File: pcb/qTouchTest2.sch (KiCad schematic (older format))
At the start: 40 parts, among them CON1 AVR-ISP-6, J1 USB-MINI-B, K1 CONN_3, P1 CONN_1, P2 CONN_1, P3 CONN_1, P6 CONN_1, P7 CONN_1, P8 CONN_1, P9 CONN_1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

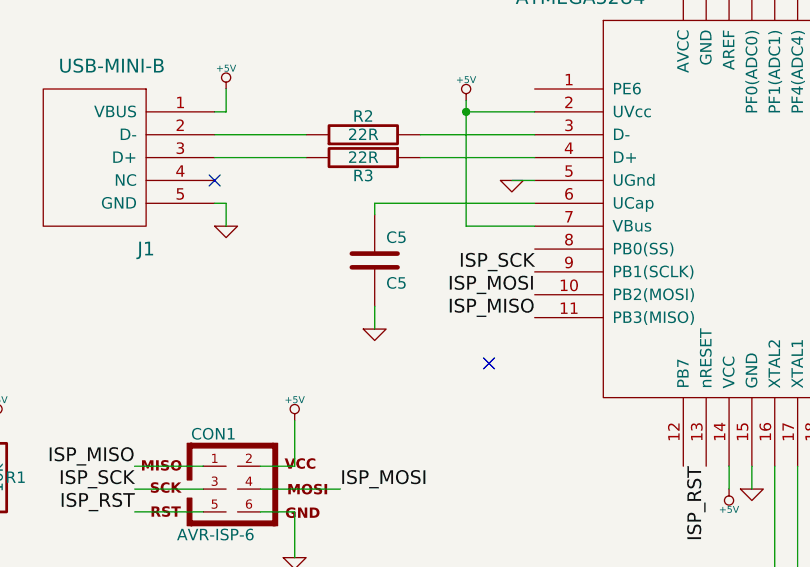
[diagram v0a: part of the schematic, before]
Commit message: adding C5 value to schematic and netlist
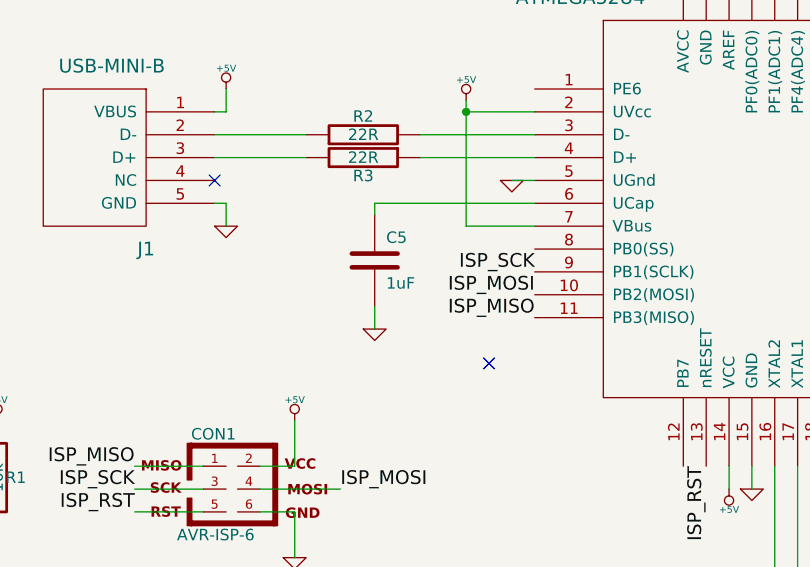
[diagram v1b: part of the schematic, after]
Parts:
- C5: value C5 -> 1uF
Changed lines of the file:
@@
-EESchema Schematic File Version 2  date Fri 04 May 2012 02:13:05 PM EEST
+EESchema Schematic File Version 2  date Wed 27 Mar 2013 18:11:13 GMT
 LIBS:power
 LIBS:device
@@
 LIBS:contrib
 LIBS:valves
-LIBS:my_parts
 LIBS:qTouchTest2-cache
 EELAYER 25  0
@@
 Sheet 1 1
 Title ""
-Date "4 may 2012"
+Date "27 mar 2013"
 Rev ""
 Comp ""
@@
 P 4050 3600
 F 0 "C5" H 4100 3700 50  0000 L CNN
-F 1 "C5" H 4100 3500 50  0000 L CNN
+F 1 "1uF" H 4100 3500 50  0000 L CNN
 	1    4050 3600
 	1    0    0    -1
